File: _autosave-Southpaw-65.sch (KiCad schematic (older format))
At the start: 205 parts, among them J1 USB_C_Receptacle_USB2.0, SW1 SW_Push, U1 ATmega32A-PU, Y1 16MHz

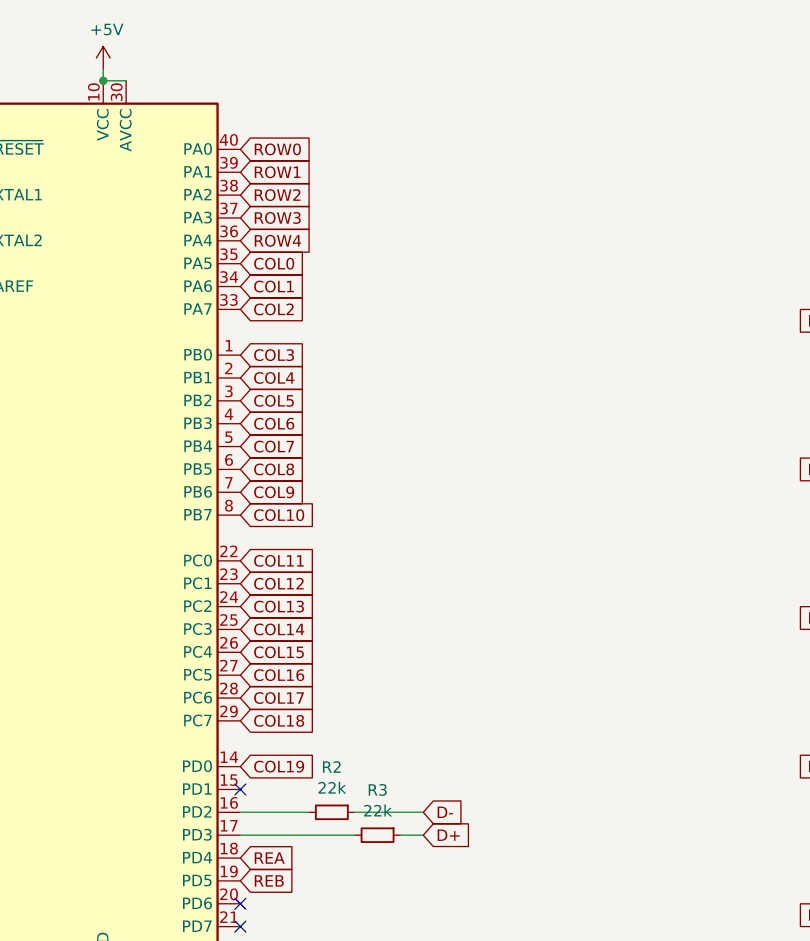
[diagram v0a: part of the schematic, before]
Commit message: Finished all connections from switches to diodes
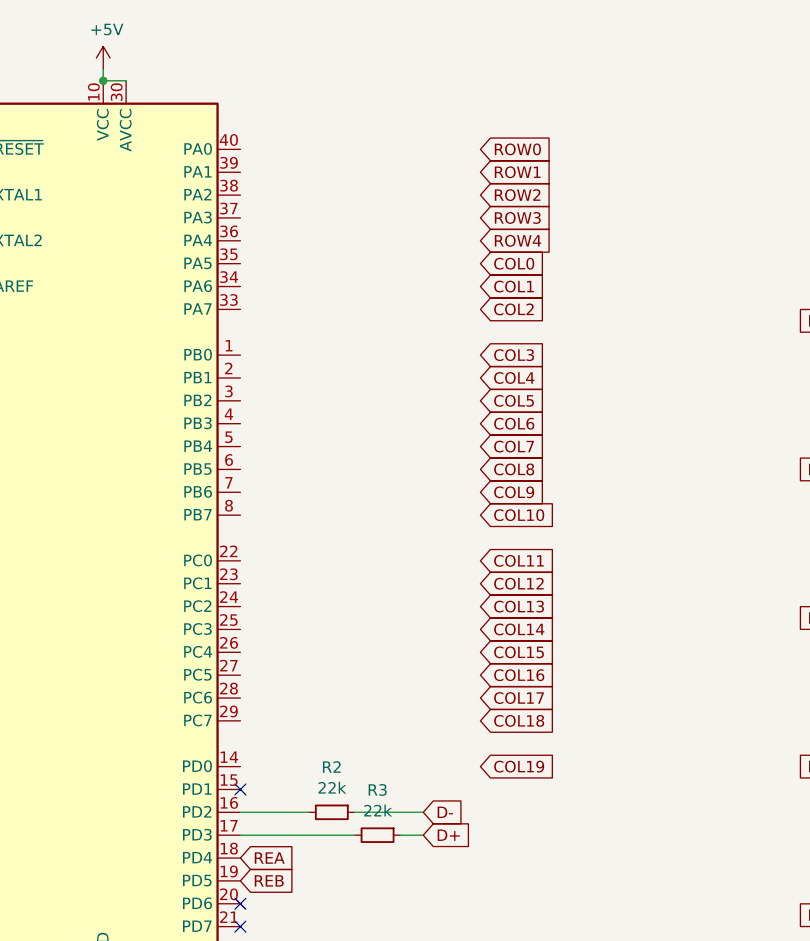
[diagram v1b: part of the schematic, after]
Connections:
- net COL0: no longer U1.35 (PA5)
- net COL1: no longer U1.34 (PA6)
- net COL10: no longer U1.8 (PB7)
- net COL11: no longer U1.22 (PC0)
- net COL12: no longer U1.23 (PC1)
- net COL13: no longer U1.24 (PC2)
- net COL14: no longer U1.25 (PC3)
- net COL15: no longer U1.26 (PC4)
- net COL16: no longer U1.27 (PC5)
- net COL17: no longer U1.28 (PC6)
- net COL18: no longer U1.29 (PC7)
- net COL19: no longer U1.14 (PD0)
- net COL2: no longer U1.33 (PA7)
- net COL3: no longer U1.1 (PB0)
- net COL4: no longer U1.2 (PB1)
- net COL5: no longer U1.3 (PB2)
- net COL6: no longer U1.4 (PB3)
- net COL7: no longer U1.5 (PB4)
- net COL8: no longer U1.6 (PB5)
- net COL9: no longer U1.7 (PB6)
- net ROW0: no longer U1.40 (PA0)
- net ROW1: no longer U1.39 (PA1)
- net ROW2: no longer U1.38 (PA2)
- net ROW3: no longer U1.37 (PA3)
- net ROW4: no longer U1.36 (PA4)
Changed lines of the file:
@@
 Wire Wire Line
 	17400 3350 17400 4000
-Text GLabel 2000 1050 2    50   Input ~ 0
+Text GLabel 3050 1050 2    50   Input ~ 0
 ROW0
-Text GLabel 2000 1150 2    50   Input ~ 0
+Text GLabel 3050 1150 2    50   Input ~ 0
 ROW1
-Text GLabel 2000 1250 2    50   Input ~ 0
+Text GLabel 3050 1250 2    50   Input ~ 0
 ROW2
-Text GLabel 2000 1350 2    50   Input ~ 0
+Text GLabel 3050 1350 2    50   Input ~ 0
 ROW3
-Text GLabel 2000 1450 2    50   Input ~ 0
+Text GLabel 3050 1450 2    50   Input ~ 0
 ROW4
-Text GLabel 2000 1550 2    50   Input ~ 0
+Text GLabel 3050 1550 2    50   Input ~ 0
 COL0
-Text GLabel 2000 1650 2    50   Input ~ 0
+Text GLabel 3050 1650 2    50   Input ~ 0
 COL1
-Text GLabel 2000 1750 2    50   Input ~ 0
+Text GLabel 3050 1750 2    50   Input ~ 0
 COL2
-Text GLabel 2000 1950 2    50   Input ~ 0
+Text GLabel 3050 1950 2    50   Input ~ 0
 COL3
-Text GLabel 2000 2050 2    50   Input ~ 0
+Text GLabel 3050 2050 2    50   Input ~ 0
 COL4
-Text GLabel 2000 2150 2    50   Input ~ 0
+Text GLabel 3050 2150 2    50   Input ~ 0
 COL5
-Text GLabel 2000 2250 2    50   Input ~ 0
+Text GLabel 3050 2250 2    50   Input ~ 0
 COL6
-Text GLabel 2000 2350 2    50   Input ~ 0
+Text GLabel 3050 2350 2    50   Input ~ 0
 COL7
-Text GLabel 2000 2450 2    50   Input ~ 0
+Text GLabel 3050 2450 2    50   Input ~ 0
 COL8
-Text GLabel 2000 2550 2    50   Input ~ 0
+Text GLabel 3050 2550 2    50   Input ~ 0
 COL9
-Text GLabel 2000 2650 2    50   Input ~ 0
+Text GLabel 3050 2650 2    50   Input ~ 0
 COL10
-Text GLabel 2000 2850 2    50   Input ~ 0
+Text GLabel 3050 2850 2    50   Input ~ 0
 COL11
-Text GLabel 2000 2950 2    50   Input ~ 0
+Text GLabel 3050 2950 2    50   Input ~ 0
 COL12
-Text GLabel 2000 3050 2    50   Input ~ 0
+Text GLabel 3050 3050 2    50   Input ~ 0
 COL13
-Text GLabel 2000 3150 2    50   Input ~ 0
+Text GLabel 3050 3150 2    50   Input ~ 0
 COL14
-Text GLabel 2000 3250 2    50   Input ~ 0
+Text GLabel 3050 3250 2    50   Input ~ 0
 COL15
-Text GLabel 2000 3350 2    50   Input ~ 0
+Text GLabel 3050 3350 2    50   Input ~ 0
 COL16
-Text GLabel 2000 3450 2    50   Input ~ 0
+Text GLabel 3050 3450 2    50   Input ~ 0
 COL17
-Text GLabel 2000 3550 2    50   Input ~ 0
+Text GLabel 3050 3550 2    50   Input ~ 0
 COL18
-Text GLabel 2000 3750 2    50   Input ~ 0
+Text GLabel 3050 3750 2    50   Input ~ 0
 COL19
 $Comp
